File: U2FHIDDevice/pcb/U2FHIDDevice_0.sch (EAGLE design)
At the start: 31 parts, among them CN1 STLINKV2_SWD_IF_, CN2 TE-1734028, SW1 SKRPACE010, SW2 SKRPACE010, U1 STM32F411RET6, U2 LD39050PU33R, U3 USBLC6-2SC6, X1 NX3215SA-32.768K

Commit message: 回路図／基板デザインを修正
・ユーザーボタンを削除（不要なので）
・通信処理中を表すLEDを追加
・プリント基板サイズを縮小
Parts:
- removed C12: 0.1uF, Parts:CAP_0603
- removed R5: 100, Parts:RESISTOR_0603
- removed SW1: SKRPACE010, Parts:SKRPACE010
- added D1: WE_150060VS55040, Parts:WE_150060VS55040
- R4: value 4.7k -> 510
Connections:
- removed net USER_BUTTON: C12.1, R4.1, SW1.P, SW1.P1, U1.PC13
- new net USER_LED: R4.1, U1.PA5
- net 0V: now also D1.C; no longer R5.2, SW1.S, SW1.S1
- net N$1: now also D1.A, R4.2; no longer C12.2, R5.1
- net VDD: no longer R4.2
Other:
- note added: "NUCLEOに付属の ST-LINK V2-1に接続します"
- note added: "U2F USB HIDデバイス"
- note added: "ファームウェア書込 ／デバッグ用回路"
- note added: "ユーザーLED （緑色）"
- note added: "試作基板回路図 Ver. 0.0"
- note added: "電源回路"
- note removed: "ユーザーボタン"
- moved on the sheet: R4

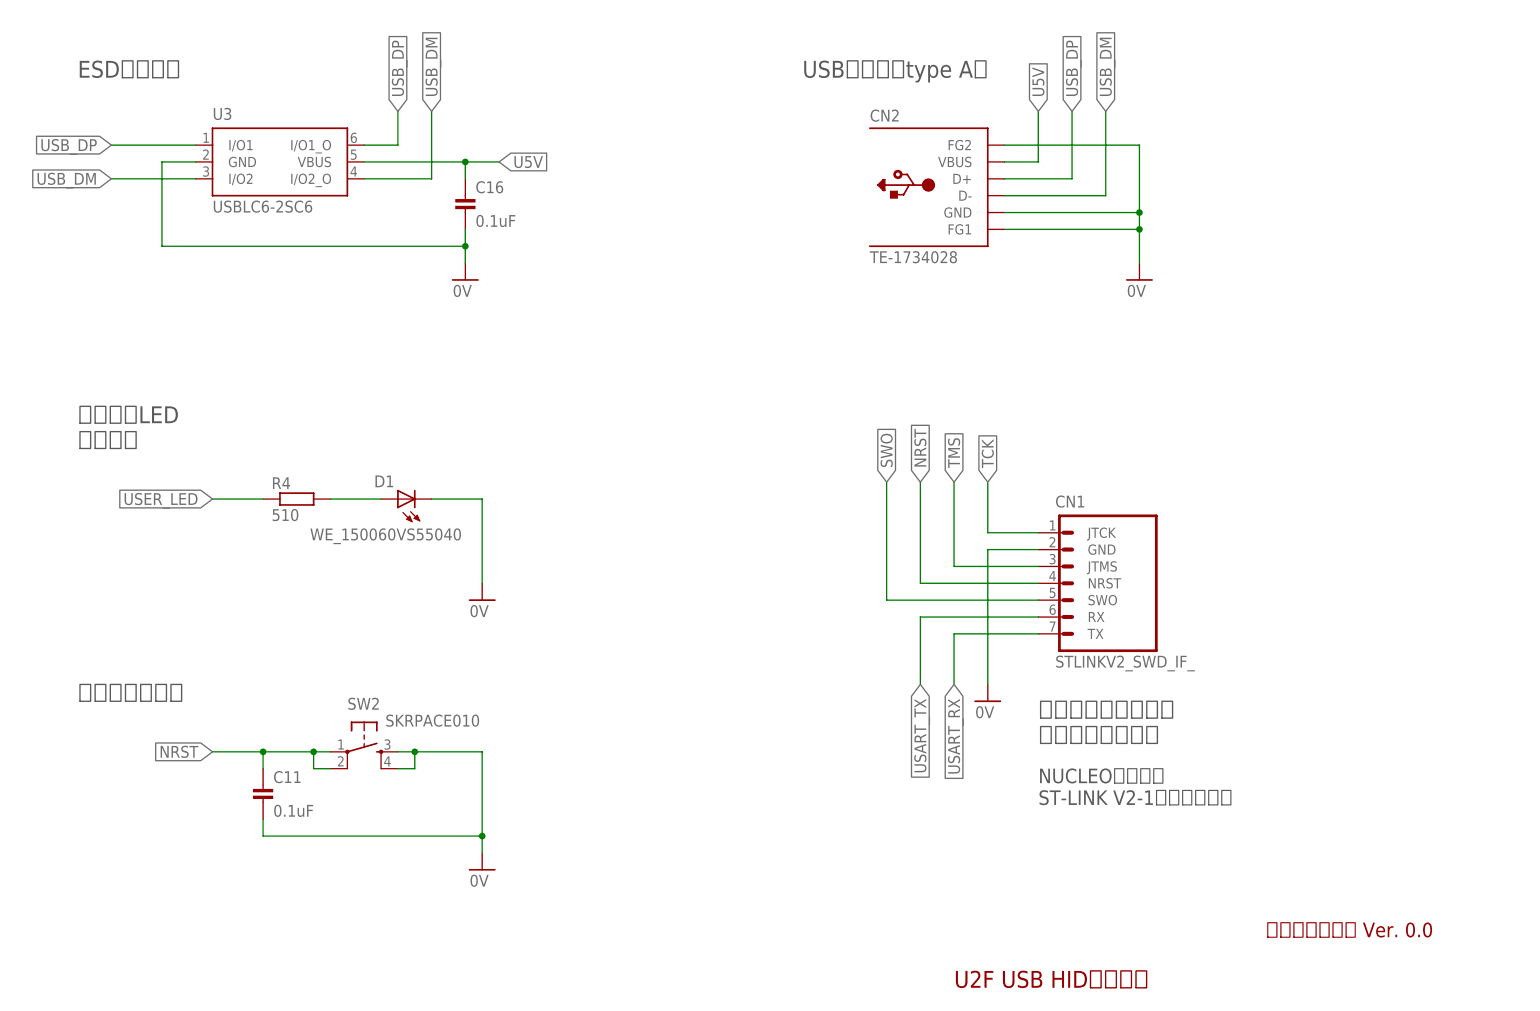
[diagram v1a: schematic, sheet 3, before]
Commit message: 回路図／基板デザインを修正
・青色LEDを追加（One Cardと通信中に点灯させる想定）
・回路が間違っていたので修正
・リセットボタン、LDOの位置を修正
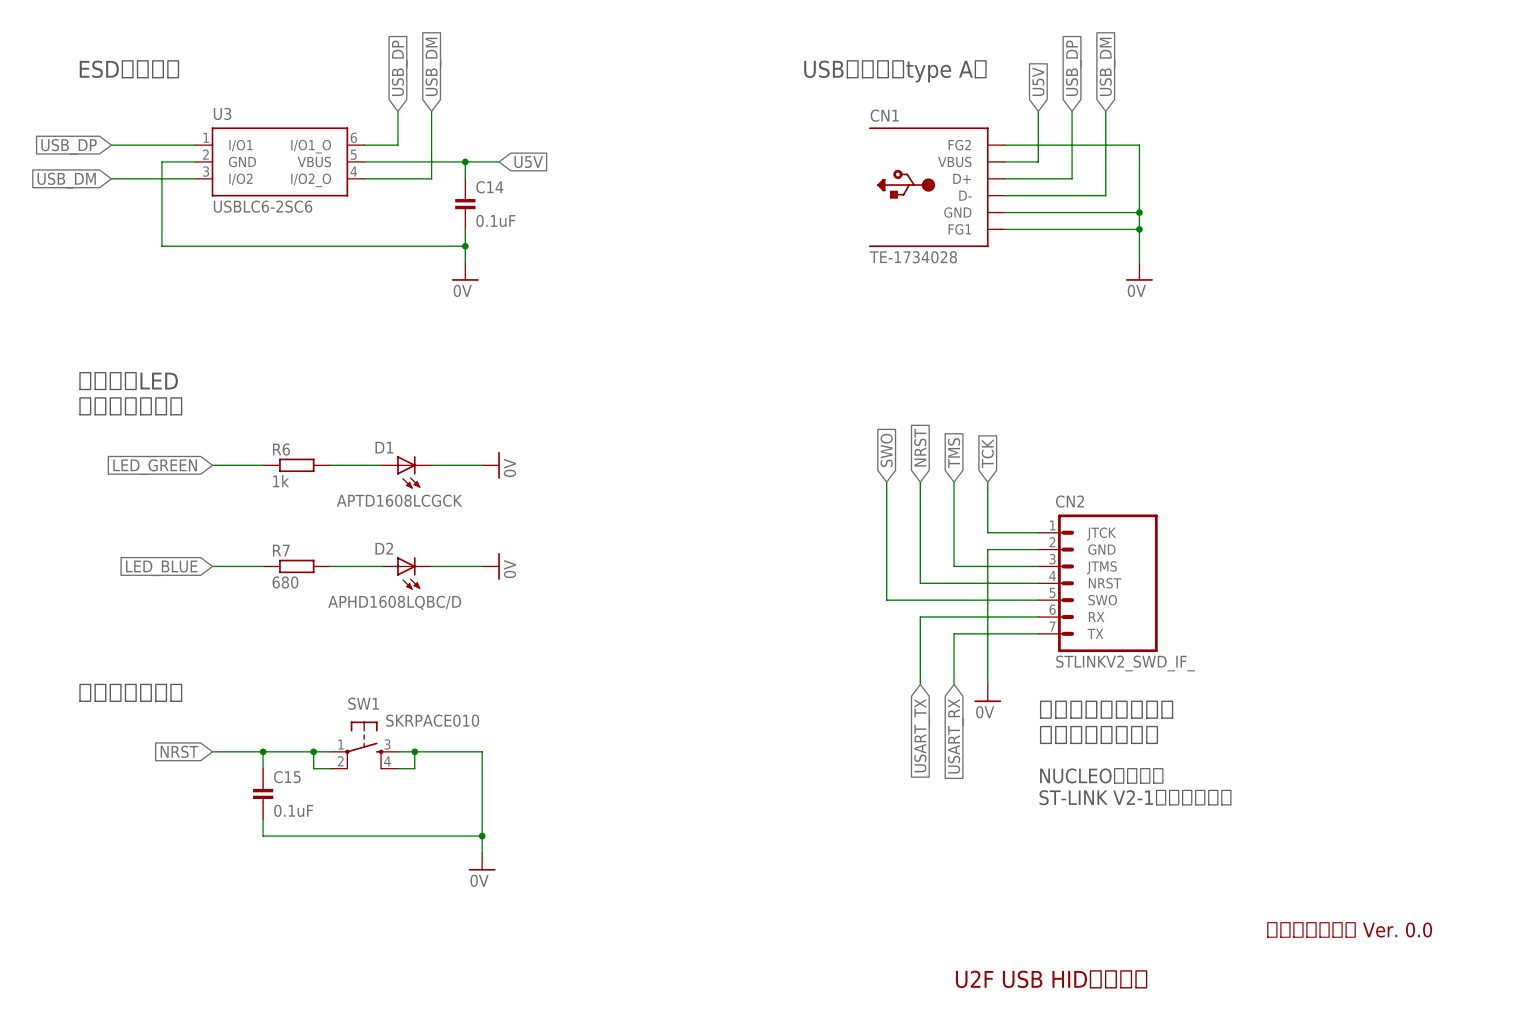
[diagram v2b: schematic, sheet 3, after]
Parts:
- removed C16: 0.1uF, Parts:CAP_0603
- added C12: 4.7uF, Parts:CAP_1206
- added D2: APHD1608LQBC/D, Parts:APHD1608LQBC/D
- added R5: 0, Parts:RESISTOR_0603
- added R7: 680, Parts:RESISTOR_0603
- C1: value 0.1uF -> 2.7pF
- C11: value 0.1uF -> 1uF
- C2: value 1uF -> 2.7pF
- C5: value 4.7uF -> 1uF; device Parts:CAP_1206 -> Parts:CAP_0603
- C6, C7: value 2.7pF -> 0.1uF
- C9: value 1uF -> 0.1uF
- CN1: value STLINKV2_SWD_IF_ -> TE-1734028; device Connectors:STLINKV2_SWD_IF_ -> Connectors:TE-1734028
- CN2: value TE-1734028 -> STLINKV2_SWD_IF_; device Connectors:TE-1734028 -> Connectors:STLINKV2_SWD_IF_
- D1: value WE_150060VS55040 -> APTD1608LCGCK; device Parts:WE_150060VS55040 -> Parts:APTD1608LCGCK
- R3: value 0 -> 10k
- R4: value 510 -> 10k
- R6: value 10k -> 1k
- renumbered SW2 to SW1
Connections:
- removed net USER_LED: R4.1, U1.PA5
- removed net VBAT: C9.1, U1.VBAT
- new net LED_BLUE: R7.1, U1.PA6
- new net LED_GREEN: R6.1, U1.PA5
- new net N$4: D2.A, R7.2
- new net USER_BUTTON: R4.1, U1.PC13
- net 0V: now also C12.2, C8.2, CN1.FG1, CN1.FG2, D2.C, R3.2, R5.1; no longer C13.2, C16.2, CN2.FG1, CN2.FG2, R3.1, R6.2
- net AGND: now also C13.2, R5.2; no longer C8.2, R3.2
- net AVDD: now also C13.1; no longer C8.1
- net BOOT0: now also R3.1; no longer R6.1
- net N$1: now also R6.2; no longer R4.2
- net N$2: now also C1.1; no longer C6.1
- net N$3: now also C2.1; no longer C7.1
- net NRST: now also C15.1, CN2.NRST; no longer C11.1, CN1.NRST
- net SWO: now also CN2.SWO; no longer CN1.SWO
- net TCK: now also CN2.JTCK; no longer CN1.JTCK
- net TMS: now also CN2.JTMS; no longer CN1.JTMS
- net U5V: now also C14.1, C3.1, C4.1, CN1.VBUS; no longer C1.1, C16.1, C2.1, CN2.VBUS
- net USART_RX: now also CN2.TX; no longer CN1.TX
- net USART_TX: now also CN2.RX; no longer CN1.RX
- net USB_DM: now also CN1.D-; no longer CN2.D-
- net USB_DP: now also CN1.D+; no longer CN2.D+
- net VCAP_1: now also C12.1; no longer C5.1
- net VDD: now also C11.1, C5.1, C6.1, C7.1, C8.1, C9.1, R4.2, U1.VBAT; no longer C13.1, C14.1, C15.1, C3.1, C4.1
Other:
- note added: "1uFはVBATの 近傍に配置"
- note added: "ユーザーLED （緑色・青色）"
- note removed: "ユーザーLED （緑色）"
- moved on the sheet: C10, C13, C3, C4, C5, C8, C9, D1

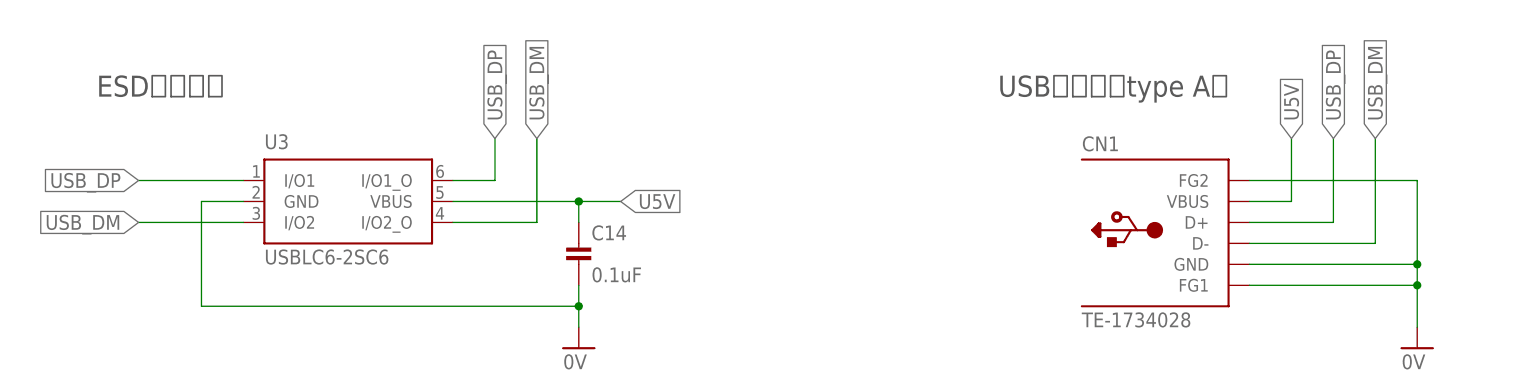
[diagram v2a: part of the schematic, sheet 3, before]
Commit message: 回路図／基板デザインを修正
・実体配線を考慮し、部品配置を修正
・配線が間違っていたので修正（ESD保護回路の部分）
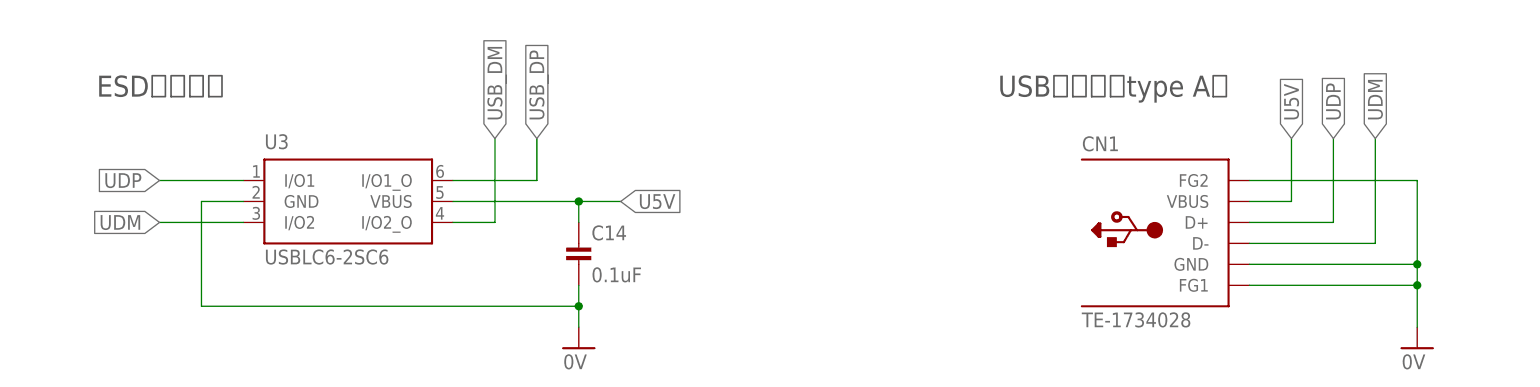
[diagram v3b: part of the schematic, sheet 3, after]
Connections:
- new net UDM: CN1.D-, U3.I/O2
- new net UDP: CN1.D+, U3.I/O1
- net USB_DM: no longer CN1.D-, U3.I/O2
- net USB_DP: no longer CN1.D+, U3.I/O1

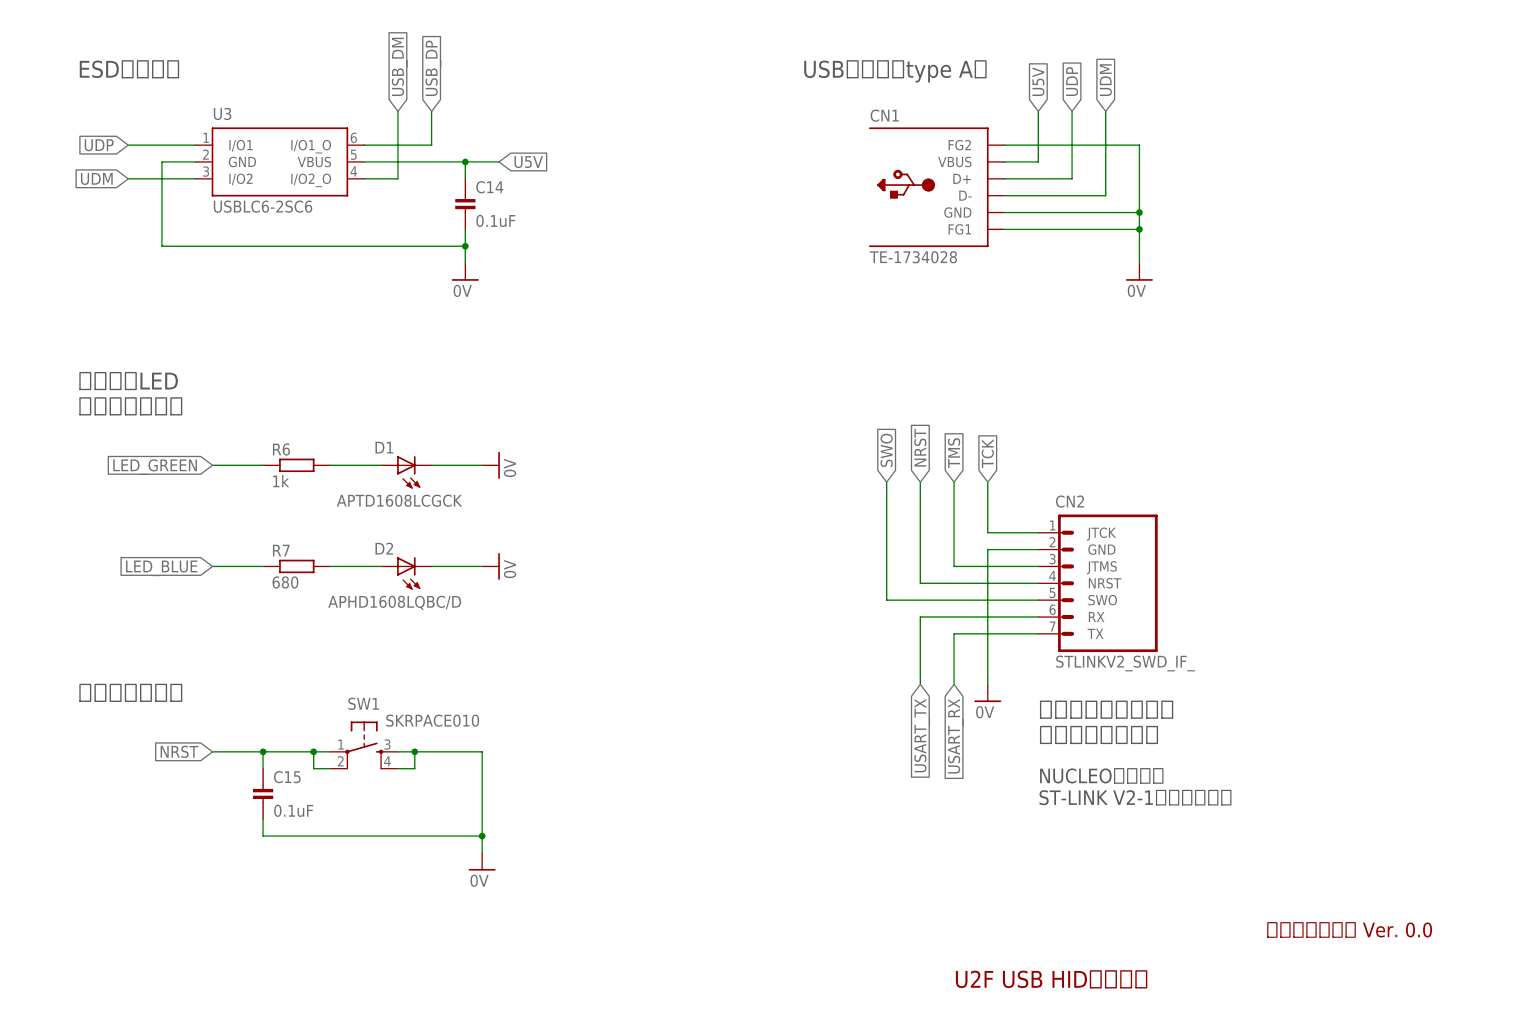
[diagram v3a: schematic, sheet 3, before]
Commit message: 回路図／基板デザインを修正
・実体配線ずみ
・ST-LINK
V2-1インターフェースを背面パッドではなく、スルーホールに修正しました（スルーホールテストワイヤーで接続可能とするための措置）
・一部IC、クリスタルのパッド面積を拡張（手はんだを可能とするための措置）
・部品表、ガーバーデータを出力
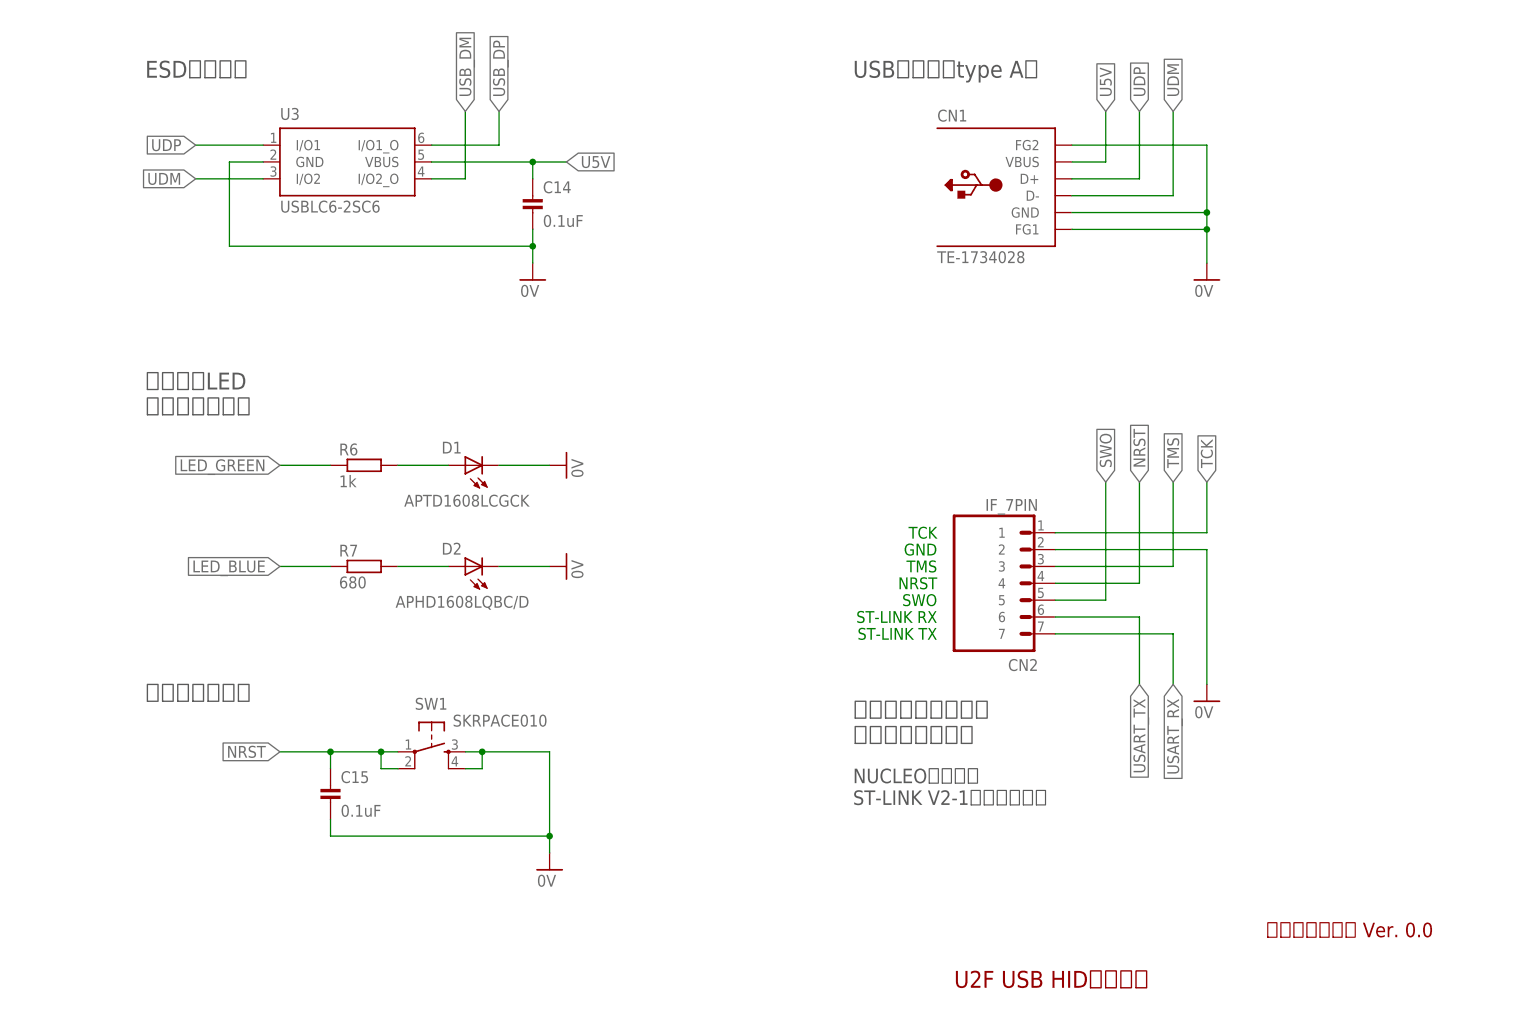
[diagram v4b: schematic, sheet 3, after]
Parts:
- CN2: value STLINKV2_SWD_IF_ -> IF_7PIN; device Connectors:STLINKV2_SWD_IF_ -> Connectors:IF_7PIN
- U1: value STM32F411RET6 -> STM32F411RET6_; device Parts:STM32F411RET6 -> Parts:STM32F411RET6_
- U2: value LD39050PU33R -> LD39050PU33R_DEV; device Parts:LD39050PU33R -> Parts:LD39050PU33R_DEV
- X1: value NX3215SA-32.768K -> NX3215SA_; device Parts:NX3215SA-32.768K -> Parts:NX3215SA_
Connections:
- net 0V: now also CN2.2; no longer CN2.GND
- net NRST: now also CN2.4; no longer CN2.NRST
- net SWO: now also CN2.5; no longer CN2.SWO
- net TCK: now also CN2.1; no longer CN2.JTCK
- net TMS: now also CN2.3; no longer CN2.JTMS
- net USART_RX: now also CN2.7; no longer CN2.TX
- net USART_TX: now also CN2.6; no longer CN2.RX
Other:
- note added: "GND"
- note added: "NRST"
- note added: "ST-LINK RX"
- note added: "ST-LINK TX"
- note added: "SWO"
- note added: "TCK"
- note added: "TMS"
- moved on the sheet: C14, C15, CN1, CN2, D1, D2, R6, R7, SW1, U3
